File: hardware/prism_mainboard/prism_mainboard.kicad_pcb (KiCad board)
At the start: 6 copper layers, 100 x 100 mm, 76 parts, among them IC1 KTDM4G3C618BGIEAT, IC2 KTDM4G3C618BGIEAT, IC3 USB3320C-EZK, J1 503398-1892, U1 XC7Z015-2CLG485I, U2 LMS7002M, U3 PEC16-4220F-S0024, U4 AMS1117-1.8, U5 AMS1117-1.8, U6 AMS1117-1.8, U7 AMS1117-1.8

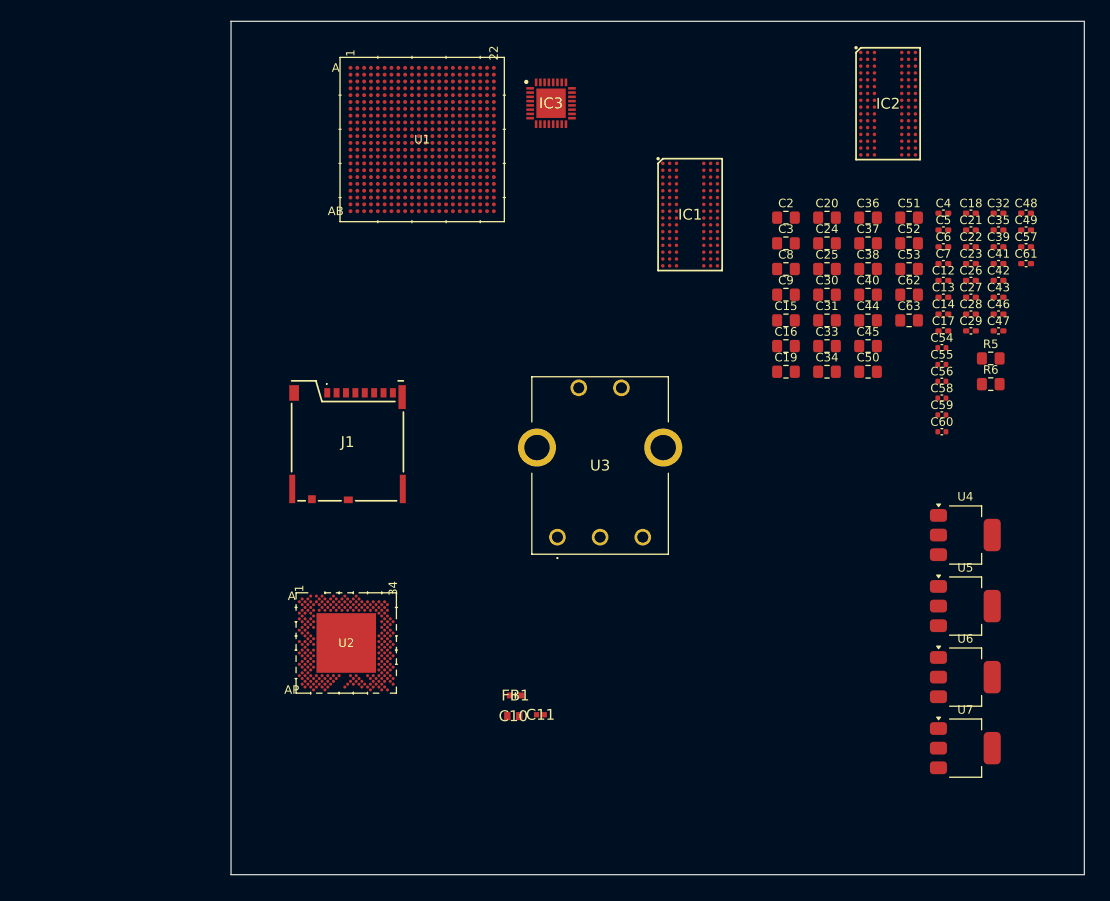
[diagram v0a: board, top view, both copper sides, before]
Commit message: Schematic and PCB Updates
Added Edge.cuts to max 100mm x 100mm size, just as a base, can shrink it if needed. Simple schematic labeling for memory and other necessary stuff.
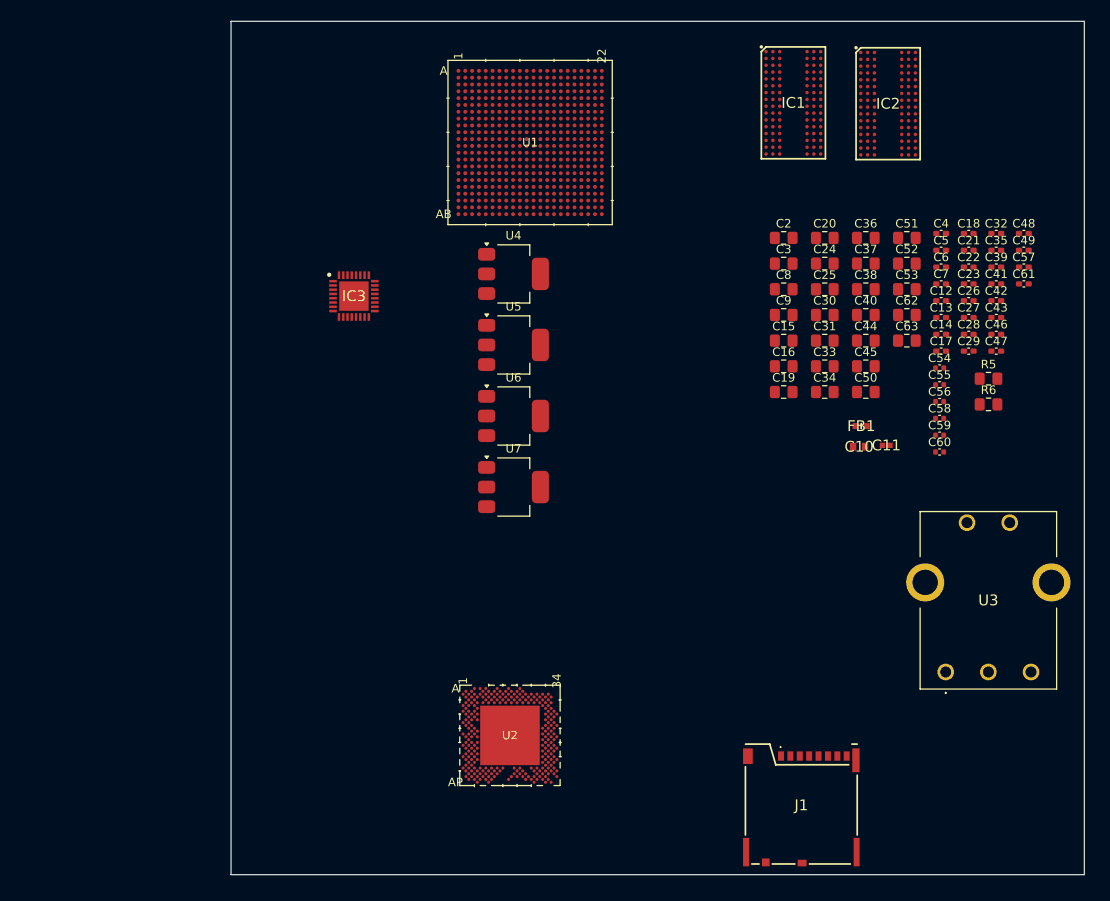
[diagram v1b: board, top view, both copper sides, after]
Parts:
- moved J1 68.1 mm to (137.9, 141.5)
- moved U5 61.2 mm to (110.8, 94.7)
- moved U6 61.2 mm to (110.8, 103.0)
- moved U4 61.2 mm to (110.8, 86.4)
- moved U7 61.2 mm to (110.8, 111.4)
- moved C11 51.4 mm to (154.4, 106.5)
- moved FB1 51.4 mm to (151.5, 104.2)
- moved C10 51.4 mm to (151.2, 106.7)
- moved U3 48.2 mm to (161.4, 133.1)
- moved IC3 32.3 mm to (92.0, 89.0)
- moved U2 22.0 mm to (110.3, 140.5)
- moved IC1 17.8 mm to (143.6, 66.3)
- moved U1 12.7 mm to (112.7, 71.0)
- moved C15 2.39 mm to (142.4, 94.2)
- moved C16 2.39 mm to (142.4, 97.2)
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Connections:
- IC1 pad A2: unconnected-(IC1-DQU5-PadA2) -> DQU5_0
- IC1 pad A3: unconnected-(IC1-DQU7-PadA3) -> DQU7_0
- IC1 pad A7: unconnected-(IC1-DQU4-PadA7) -> DQU4_0
- IC1 pad B7: unconnected-(IC1-~{DQSU}-PadB7) -> DQSUN_0
- IC1 pad B8: unconnected-(IC1-DQU6-PadB8) -> DQU6_0
- IC1 pad C2: unconnected-(IC1-DQU3-PadC2) -> DQU3_0
- IC1 pad C3: unconnected-(IC1-DQU1-PadC3) -> DQU1_0
- IC1 pad C7: unconnected-(IC1-DQSU-PadC7) -> DQSUP_0
- IC1 pad C8: unconnected-(IC1-DQU2-PadC8) -> DQU2_0
- IC1 pad D3: unconnected-(IC1-DMU-PadD3) -> DM1
- IC1 pad D7: unconnected-(IC1-DQU0-PadD7) -> DQU0_0
- IC1 pad E3: unconnected-(IC1-DQL0-PadE3) -> DQL0_0
- IC1 pad E7: unconnected-(IC1-DML-PadE7) -> DM0
- IC1 pad F2: unconnected-(IC1-DQL2-PadF2) -> DQL2_0
- IC1 pad F3: unconnected-(IC1-DQSL-PadF3) -> DQSLP_0
- IC1 pad F7: unconnected-(IC1-DQL1-PadF7) -> DQL1_0
- IC1 pad F8: unconnected-(IC1-DQL3-PadF8) -> DQL3_0
- IC1 pad G2: unconnected-(IC1-DQL6-PadG2) -> DQL6_0
- IC1 pad G3: unconnected-(IC1-~{DQSL}-PadG3) -> DQSLN_0
- IC1 pad H3: unconnected-(IC1-DQL4-PadH3) -> DQL4_0
- IC1 pad H7: unconnected-(IC1-DQL7-PadH7) -> DQL7_0
- IC1 pad H8: unconnected-(IC1-DQL5-PadH8) -> DQL5_0
- IC1 pad J3: unconnected-(IC1-~{RAS}-PadJ3) -> RAS
- IC1 pad J7: unconnected-(IC1-CK-PadJ7) -> CKP
- IC1 pad K1: unconnected-(IC1-ODT-PadK1) -> ODT
- IC1 pad K3: unconnected-(IC1-~{CAS}-PadK3) -> CAS
- IC1 pad K7: unconnected-(IC1-~{CK}-PadK7) -> CKN
- IC1 pad K9: unconnected-(IC1-CKE-PadK9) -> CKE
- IC1 pad L2: unconnected-(IC1-~{CS}-PadL2) -> CS
- IC1 pad L3: unconnected-(IC1-~{WE}-PadL3) -> WE
- IC1 pad L7: unconnected-(IC1-A10/AP-PadL7) -> A10
- IC1 pad M2: unconnected-(IC1-BA0-PadM2) -> BA0
- IC1 pad M3: unconnected-(IC1-BA2-PadM3) -> BA
- IC1 pad N2: unconnected-(IC1-A3-PadN2) -> A3
- IC1 pad N3: unconnected-(IC1-A0-PadN3) -> A0
- IC1 pad N7: unconnected-(IC1-A12/~{BC}-PadN7) -> A12
- IC1 pad N8: unconnected-(IC1-BA1-PadN8) -> BA1
- IC1 pad P2: unconnected-(IC1-A5-PadP2) -> A5
- IC1 pad P3: unconnected-(IC1-A2-PadP3) -> A2
- IC1 pad P7: unconnected-(IC1-A1-PadP7) -> A1
- IC1 pad P8: unconnected-(IC1-A4-PadP8) -> A4
- IC1 pad R2: unconnected-(IC1-A7-PadR2) -> A7
- IC1 pad R3: unconnected-(IC1-A9-PadR3) -> A9
- IC1 pad R7: unconnected-(IC1-A11-PadR7) -> A11
- IC1 pad R8: unconnected-(IC1-A6-PadR8) -> A6
- IC1 pad T3: unconnected-(IC1-A13-PadT3) -> A13
- IC1 pad T7: unconnected-(IC1-A14-PadT7) -> A14
- IC1 pad T8: unconnected-(IC1-A8-PadT8) -> A8
- IC2 pad A2: unconnected-(IC2-DQU5-PadA2) -> DQU5_1
- IC2 pad A3: unconnected-(IC2-DQU7-PadA3) -> DQU7_1
- IC2 pad A7: unconnected-(IC2-DQU4-PadA7) -> DQU4_1
- IC2 pad B7: unconnected-(IC2-~{DQSU}-PadB7) -> DQSUN_1
- IC2 pad B8: unconnected-(IC2-DQU6-PadB8) -> DQU6_1
- IC2 pad C2: unconnected-(IC2-DQU3-PadC2) -> DQU3_1
- IC2 pad C3: unconnected-(IC2-DQU1-PadC3) -> DQU1_1
- IC2 pad C7: unconnected-(IC2-DQSU-PadC7) -> DQSUP_1
- IC2 pad C8: unconnected-(IC2-DQU2-PadC8) -> DQU2_1
- IC2 pad D3: unconnected-(IC2-DMU-PadD3) -> DM3
- IC2 pad D7: unconnected-(IC2-DQU0-PadD7) -> DQU0_1
- IC2 pad E3: unconnected-(IC2-DQL0-PadE3) -> DQL0_1
- IC2 pad E7: unconnected-(IC2-DML-PadE7) -> DM2
- IC2 pad F2: unconnected-(IC2-DQL2-PadF2) -> DQL2_1
- IC2 pad F3: unconnected-(IC2-DQSL-PadF3) -> DQSLP_1
- IC2 pad F7: unconnected-(IC2-DQL1-PadF7) -> DQL1_1
- IC2 pad F8: unconnected-(IC2-DQL3-PadF8) -> DQL3_1
- IC2 pad G2: unconnected-(IC2-DQL6-PadG2) -> DQL6_1
- IC2 pad G3: unconnected-(IC2-~{DQSL}-PadG3) -> DQSLN_1
- IC2 pad H3: unconnected-(IC2-DQL4-PadH3) -> DQL4_1
- IC2 pad H7: unconnected-(IC2-DQL7-PadH7) -> DQL7_1
- IC2 pad H8: unconnected-(IC2-DQL5-PadH8) -> DQL5_1
- IC2 pad J3: unconnected-(IC2-~{RAS}-PadJ3) -> RAS
- IC2 pad J7: unconnected-(IC2-CK-PadJ7) -> CKP
- IC2 pad K1: unconnected-(IC2-ODT-PadK1) -> ODT
- IC2 pad K3: unconnected-(IC2-~{CAS}-PadK3) -> CAS
- IC2 pad K7: unconnected-(IC2-~{CK}-PadK7) -> CKN
- IC2 pad K9: unconnected-(IC2-CKE-PadK9) -> CKE
- IC2 pad L2: unconnected-(IC2-~{CS}-PadL2) -> CS
- IC2 pad L3: unconnected-(IC2-~{WE}-PadL3) -> WE
- IC2 pad L7: unconnected-(IC2-A10/AP-PadL7) -> A10
- IC2 pad M2: unconnected-(IC2-BA0-PadM2) -> BA0
- IC2 pad M3: unconnected-(IC2-BA2-PadM3) -> BA
- IC2 pad N2: unconnected-(IC2-A3-PadN2) -> A3
- IC2 pad N3: unconnected-(IC2-A0-PadN3) -> A0
- IC2 pad N7: unconnected-(IC2-A12/~{BC}-PadN7) -> A12
- IC2 pad N8: unconnected-(IC2-BA1-PadN8) -> BA1
- IC2 pad P2: unconnected-(IC2-A5-PadP2) -> A5
- IC2 pad P3: unconnected-(IC2-A2-PadP3) -> A2
- IC2 pad P7: unconnected-(IC2-A1-PadP7) -> A1
- IC2 pad P8: unconnected-(IC2-A4-PadP8) -> A4
- IC2 pad R2: unconnected-(IC2-A7-PadR2) -> A7
- IC2 pad R3: unconnected-(IC2-A9-PadR3) -> A9
- IC2 pad R7: unconnected-(IC2-A11-PadR7) -> A11
- IC2 pad R8: unconnected-(IC2-A6-PadR8) -> A6
- IC2 pad T3: unconnected-(IC2-A13-PadT3) -> A13
- IC2 pad T7: unconnected-(IC2-A14-PadT7) -> A14
- IC2 pad T8: unconnected-(IC2-A8-PadT8) -> A8
- U1 pad AA22: unconnected-(U1E-PS_DDR_DQ26_502-PadAA22) -> DQU2_1
- U1 pad B21: unconnected-(U1C-PS_DDR_DQ2_502-PadB21) -> DQL2_0
- U1 pad B22: unconnected-(U1C-PS_DDR_DM0_502-PadB22) -> DM0
- U1 pad C20: unconnected-(U1C-PS_DDR_DQ1_502-PadC20) -> DQL1_0
- U1 pad C21: unconnected-(U1C-PS_DDR_DQS_P0_502-PadC21) -> DQSLP_0
- U1 pad D20: unconnected-(U1C-PS_DDR_DQ3_502-PadD20) -> DQL3_0
- U1 pad D21: unconnected-(U1C-PS_DDR_DQS_N0_502-PadD21) -> DQSLN_0
- U1 pad D22: unconnected-(U1C-PS_DDR_DQ0_502-PadD22) -> DQL0_0
- U1 pad E20: unconnected-(U1C-PS_DDR_DQ4_502-PadE20) -> DQL4_0
- U1 pad E22: unconnected-(U1C-PS_DDR_DQ5_502-PadE22) -> DQL5_0
- U1 pad F16: unconnected-(U1C-PS_CLK_500-PadF16) -> CLK
- U1 pad F19: unconnected-(U1C-PS_DDR_A13_502-PadF19) -> A13
- U1 pad F21: unconnected-(U1C-PS_DDR_DQ6_502-PadF21) -> DQL6_0
- U1 pad F22: unconnected-(U1C-PS_DDR_DQ7_502-PadF22) -> DQL7_0
- U1 pad G18: unconnected-(U1C-PS_DDR_A11_502-PadG18) -> A11
- U1 pad G19: unconnected-(U1C-PS_DDR_A14_502-PadG19) -> A14
- U1 pad G21: unconnected-(U1C-PS_DDR_DQ8_502-PadG21) -> DQU0_0
- U1 pad G22: unconnected-(U1C-PS_DDR_DQ9_502-PadG22) -> DQU1_0
- U1 pad H18: unconnected-(U1D-PS_DDR_A9_502-PadH18) -> A9
- U1 pad H19: unconnected-(U1D-PS_DDR_A12_502-PadH19) -> A12
- U1 pad H21: unconnected-(U1D-PS_DDR_DQS_P1_502-PadH21) -> DQSUP_0
- U1 pad J16: unconnected-(U1D-PS_DDR_A6_502-PadJ16) -> A6
- U1 pad J17: unconnected-(U1D-PS_DDR_A7_502-PadJ17) -> A7
- U1 pad J18: unconnected-(U1D-PS_DDR_A8_502-PadJ18) -> A8
- U1 pad J20: unconnected-(U1D-PS_DDR_A10_502-PadJ20) -> A10
- U1 pad J21: unconnected-(U1D-PS_DDR_DQS_N1_502-PadJ21) -> DQSUN_0
- U1 pad J22: unconnected-(U1D-PS_DDR_DQ14_502-PadJ22) -> DQU6_0
- U1 pad K17: unconnected-(U1D-PS_DDR_A4_502-PadK17) -> A4
- U1 pad K18: unconnected-(U1D-PS_DDR_A5_502-PadK18) -> A5
- U1 pad K19: unconnected-(U1D-PS_DDR_A2_502-PadK19) -> A2
- U1 pad K20: unconnected-(U1D-PS_DDR_DQ15_502-PadK20) -> DQU7_0
- U1 pad K22: unconnected-(U1D-PS_DDR_DQ13_502-PadK22) -> DQU5_0
- U1 pad L16: unconnected-(U1D-PS_DDR_BA0_502-PadL16) -> BA0
- U1 pad L17: unconnected-(U1D-PS_DDR_BA1_502-PadL17) -> BA1
- U1 pad L19: unconnected-(U1D-PS_DDR_A3_502-PadL19) -> A3
- U1 pad L20: unconnected-(U1D-PS_DDR_DQ12_502-PadL20) -> DQU4_0
- U1 pad L21: unconnected-(U1D-PS_DDR_DQ11_502-PadL21) -> DQU3_0
- U1 pad L22: unconnected-(U1D-PS_DDR_DQ10_502-PadL22) -> DQU2_0
- U1 pad M17: unconnected-(U1D-PS_DDR_BA2_502-PadM17) -> BA2
- U1 pad M18: unconnected-(U1D-PS_DDR_A1_502-PadM18) -> A1
- U1 pad M19: unconnected-(U1D-PS_DDR_A0_502-PadM19) -> A0
- U1 pad M21: unconnected-(U1D-PS_DDR_DQ22_502-PadM21) -> DQL6_1
- U1 pad M22: unconnected-(U1D-PS_DDR_DQ16_502-PadM22) -> DQL0_1
- U1 pad N18: unconnected-(U1D-PS_DDR_CKN_502-PadN18) -> CKN
- U1 pad N19: unconnected-(U1D-PS_DDR_CKP_502-PadN19) -> CKP
- U1 pad N20: unconnected-(U1D-PS_DDR_DQ18_502-PadN20) -> DQL2_1
- U1 pad N21: unconnected-(U1D-PS_DDR_DQS_P2_502-PadN21) -> DQSLP_1
- U1 pad P17: unconnected-(U1D-PS_DDR_CS_B_502-PadP17) -> CS
- U1 pad P18: unconnected-(U1D-PS_DDR_ODT_502-PadP18) -> ODT
- U1 pad P20: unconnected-(U1D-PS_DDR_CAS_B_502-PadP20) -> CAS
- U1 pad P21: unconnected-(U1D-PS_DDR_DQS_N2_502-PadP21) -> DQSLN_1
- U1 pad P22: unconnected-(U1D-PS_DDR_DM2_502-PadP22) -> DM2
- U1 pad R18: unconnected-(U1E-PS_DDR_RAS_B_502-PadR18) -> RAS
- U1 pad R19: unconnected-(U1E-PS_DDR_WE_B_502-PadR19) -> WE
- U1 pad R20: unconnected-(U1E-PS_DDR_DQ20_502-PadR20) -> DQL4_1
- U1 pad R22: unconnected-(U1E-PS_DDR_DQ23_502-PadR22) -> DQL7_1
- U1 pad T19: unconnected-(U1E-PS_DDR_CKE_502-PadT19) -> CKE
- U1 pad T20: unconnected-(U1E-PS_DDR_DQ17_502-PadT20) -> DQL1_1
- U1 pad T21: unconnected-(U1E-PS_DDR_DQ21_502-PadT21) -> DQL5_1
- U1 pad T22: unconnected-(U1E-PS_DDR_DQ19_502-PadT22) -> DQL3_1
- U1 pad U21: unconnected-(U1E-PS_DDR_DQ27_502-PadU21) -> DQU3_1
- U1 pad U22: unconnected-(U1E-PS_DDR_DQ25_502-PadU22) -> DQU1_1
- U1 pad V20: unconnected-(U1E-PS_DDR_DQ30_502-PadV20) -> DQU6_1
- U1 pad V21: unconnected-(U1E-PS_DDR_DQS_P3_502-PadV21) -> DQSUP_1
- U1 pad W20: unconnected-(U1E-PS_DDR_DQ29_502-PadW20) -> DQU5_1
- U1 pad W21: unconnected-(U1E-PS_DDR_DQS_N3_502-PadW21) -> DQSUN_1
- U1 pad W22: unconnected-(U1E-PS_DDR_DQ28_502-PadW22) -> DQU4_1
- U1 pad Y20: unconnected-(U1E-PS_DDR_DQ24_502-PadY20) -> DQU0_1
- U1 pad Y22: unconnected-(U1E-PS_DDR_DQ31_502-PadY22) -> DQU7_1

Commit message: Schematic Updates
Added the LMS7002M to XC7Z015 connections, atleast the preliminary data connections.
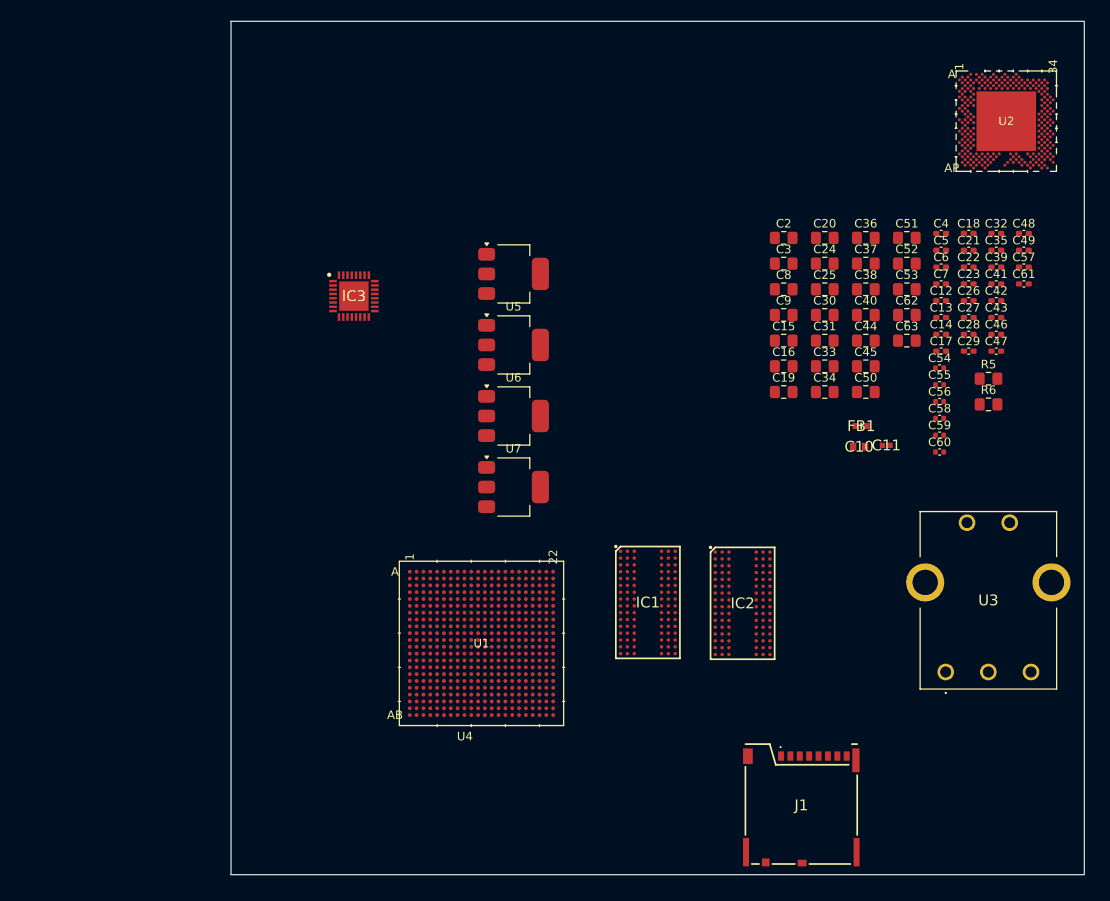
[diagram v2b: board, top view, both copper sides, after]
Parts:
- moved U2 92.5 mm to (168.5, 68.5)
- moved IC1 61.0 mm to (126.5, 124.9)
- moved IC2 61.0 mm to (137.6, 125.0)
- moved U1 59.0 mm to (107.0, 129.7)
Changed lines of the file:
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@@
 	(footprint "SamacSys_Parts:BGA96C80P9X16_750X1300X100"
 		(layer "F.Cu")
-		(at 154.65 66.45)
+		(at 137.6 125)
 		(descr "96 ball BGA-1")
 		(tags "Integrated Circuit")
@@
 		(tags "CMS SOT")
 		(property "Reference" "U4"
-			(at 0 -4.5 0)
+			(at -5.700001 54.200002 0)
 			(layer "F.SilkS")
 			(effects
@@
 	(footprint "LMS7002M:AQFN261_11P5X11P5_LIM"
 		(layer "F.Cu")
-		(at 110.336499 140.478501)
+		(at 168.5 68.5)
 		(tags "LMS7002M ")
 		(property "Reference" "U2"
@@
 	(footprint "SamacSys_Parts:BGA96C80P9X16_750X1300X100"
 		(layer "F.Cu")
-		(at 143.55 66.35)
+		(at 126.5 124.9)
 		(descr "96 ball BGA-1")
 		(tags "Integrated Circuit")
@@
 	(footprint "footprints:CLG485_XIL"
 		(layer "F.Cu")
-		(at 112.700001 70.999999)
+		(at 107 129.700001)
 		(tags "XC7Z015-2CLG485I ")
 		(property "Reference" "U1"

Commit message: Updates
Mostly Schematic updates, nothing too big. Added a few datasheets
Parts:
- added C1: T494D337K010AT, SamacSys_Parts:T494D, F.Cu at (149.8, 65.8)
- added J2: UJ32-21-C-H-G-HMT-LT-P24-TR, LIB_UJ32-21-C-H-G-HMT-LT-P24-TR:UJ3221CHGHMTLTP24TR, F.Cu at (87.2, 150.7)
- added R1: R, Resistor_SMD:R_0805_2012Metric_Pad1.20x1.40mm_HandSolder, F.Cu at (141.7, 63.6)
- added R2: R, Resistor_SMD:R_0805_2012Metric_Pad1.20x1.40mm_HandSolder, F.Cu at (141.7, 66.5)
- added R3: R, Resistor_SMD:R_0805_2012Metric_Pad1.20x1.40mm_HandSolder, F.Cu at (141.7, 69.5)
- added R4: R, Resistor_SMD:R_0805_2012Metric_Pad1.20x1.40mm_HandSolder, F.Cu at (151.4, 71.9)
- moved U7 44.4 mm to (121.5, 68.3), turned to 90 degrees
- moved IC1 39.2 mm to (133.2, 86.2)
- moved U6 34.8 mm to (113.1, 68.3), turned to 90 degrees
- moved U1 33.8 mm to (112.6, 96.4)
- moved U5 27.1 mm to (104.8, 68.3), turned to 90 degrees
- moved IC3 23.3 mm to (113.2, 79.3)
- moved U4 23.1 mm to (96.5, 68.3), turned to 90 degrees
- moved IC2 22.8 mm to (133.4, 102.5)
- moved C15 2.69 mm to (145.1, 94.2)
- moved C16 2.69 mm to (145.1, 97.2)
- moved C19 2.69 mm to (145.1, 100.2)
- moved C2 2.69 mm to (145.1, 82.2)
- moved C3 2.69 mm to (145.1, 85.2)
- moved C32 2.69 mm to (170.0, 81.7)
- moved C35 2.69 mm to (170.0, 83.6)
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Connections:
- IC3 pad 1: unconnected-(IC3-CLKOUT-Pad1) -> CLKOUT
- IC3 pad 10: unconnected-(IC3-DATA6-Pad10) -> USB_D6
- IC3 pad 13: unconnected-(IC3-DATA7-Pad13) -> USB_D7
- IC3 pad 18: unconnected-(IC3-DP-Pad18) -> Data+
- IC3 pad 19: unconnected-(IC3-DM-Pad19) -> Data-
- IC3 pad 2: unconnected-(IC3-NXT-Pad2) -> NXT
- IC3 pad 27: unconnected-(IC3-RESETB-Pad27) -> RST_B
- IC3 pad 29: unconnected-(IC3-STP-Pad29) -> STP
- IC3 pad 3: unconnected-(IC3-DATA0-Pad3) -> USB_D0
- IC3 pad 31: unconnected-(IC3-DIR-Pad31) -> DIR
- IC3 pad 4: unconnected-(IC3-DATA1-Pad4) -> USB_D1
- IC3 pad 5: unconnected-(IC3-DATA2-Pad5) -> USB_D2
- IC3 pad 6: unconnected-(IC3-DATA3-Pad6) -> USB_D3
- IC3 pad 7: unconnected-(IC3-DATA4-Pad7) -> USB_D4
- IC3 pad 9: unconnected-(IC3-DATA5-Pad9) -> USB_D5
- J1 pad 1: unconnected-(J1-DAT2-Pad1) -> SD_D2
- J1 pad 2: unconnected-(J1-CD/DAT3-Pad2) -> SD_D3
- J1 pad 3: unconnected-(J1-CMD-Pad3) -> SD_CMD
- J1 pad 5: unconnected-(J1-CLK-Pad5) -> SD_CLK
- J1 pad 6: unconnected-(J1-VSS-Pad6) -> GND
- J1 pad 7: unconnected-(J1-DAT0-Pad7) -> SD_D0
- J1 pad 8: unconnected-(J1-DAT1-Pad8) -> SD_D1
- U1 pad A11: unconnected-(U1B-PS_MIO28_501-PadA11) -> USB_D4
- U1 pad A12: unconnected-(U1B-PS_MIO30_501-PadA12) -> STP
- U1 pad A14: unconnected-(U1B-PS_MIO36_501-PadA14) -> CLKOUT
- U1 pad B11: unconnected-(U1C-PS_MIO34_501-PadB11) -> USB_D3
- U1 pad B12: unconnected-(U1C-PS_MIO43_501-PadB12) -> SD_D1
- U1 pad B14: unconnected-(U1C-PS_MIO45_501-PadB14) -> SD_D3
- U1 pad B9: unconnected-(U1A-PS_MIO37_501-PadB9) -> USB_D5
- U1 pad C10: unconnected-(U1C-PS_MIO39_501-PadC10) -> USB_D7
- U1 pad C15: unconnected-(U1C-PS_MIO41_501-PadC15) -> SD_CMD
- U1 pad C16: unconnected-(U1C-PS_MIO32_501-PadC16) -> USB_D0
- U1 pad C3: unconnected-(U1A-IO_L14N_T2_AD4N_SRCC_35-PadC3) -> FCLK1
- U1 pad D15: unconnected-(U1C-PS_MIO42_501-PadD15) -> SD_D0
- U1 pad D3: unconnected-(U1A-IO_L14P_T2_AD4P_SRCC_35-PadD3) -> MCLK1
- U1 pad D6: unconnected-(U1A-IO_L2N_T0_AD8N_35-PadD6) -> DIQ1_D4
- U1 pad D7: unconnected-(U1A-IO_L2P_T0_AD8P_35-PadD7) -> DIQ1_D5
- U1 pad D8: unconnected-(U1A-IO_L3N_T0_DQS_AD1N_35-PadD8) -> DIQ1_D6
- U1 pad E10: unconnected-(U1C-PS_MIO44_501-PadE10) -> SD_D2
- U1 pad E15: unconnected-(U1C-PS_MIO29_501-PadE15) -> DIR
- U1 pad E5: unconnected-(U1A-IO_L5N_T0_AD9N_35-PadE5) -> DIQ1_D10
- U1 pad E7: unconnected-(U1A-IO_L1N_T0_AD0N_35-PadE7) -> DIQ1_D2
- U1 pad E8: unconnected-(U1A-IO_L3P_T0_DQS_AD1P_35-PadE8) -> DIQ1_D7
- U1 pad E9: unconnected-(U1A-PS_MIO40_501-PadE9) -> SD_CLK
- U1 pad F10: unconnected-(U1C-PS_MIO38_501-PadF10) -> USB_D6
- U1 pad F14: unconnected-(U1C-PS_MIO31_501-PadF14) -> NXT
- U1 pad F5: unconnected-(U1A-IO_L5P_T0_AD9P_35-PadF5) -> DIQ1_D11
- U1 pad F6: unconnected-(U1A-IO_L6N_T0_VREF_35-PadF6) -> EN_IQSEL1
- U1 pad F7: unconnected-(U1A-IO_L1P_T0_AD0P_35-PadF7) -> DIQ1_D3
- U1 pad F9: unconnected-(U1A-PS_MIO35_501-PadF9) -> USB_D3
- U1 pad G11: unconnected-(U1C-PS_MIO33_501-PadG11) -> USB_D2
- U1 pad G6: unconnected-(U1A-IO_L6P_T0_35-PadG6) -> TXNRX1
- U1 pad G7: unconnected-(U1A-IO_L4N_T0_35-PadG7) -> DIQ1_D8
- U1 pad G8: unconnected-(U1A-IO_L4P_T0_35-PadG8) -> DIQ1_D9
- U1 pad H5: unconnected-(U1A-IO_25_35-PadH5) -> DIQ1_D1
- U1 pad H6: unconnected-(U1A-IO_0_35-PadH6) -> DIQ1_D0
- U1 pad H8: unconnected-(U1A-IO_0_34-PadH8) -> DIQ2_D0
- U1 pad J1: unconnected-(U1A-IO_L8N_T1_34-PadJ1) -> DIQ2_D10
- U1 pad J2: unconnected-(U1A-IO_L8P_T1_34-PadJ2) -> DIQ2_D11
- U1 pad J3: unconnected-(U1A-IO_L9P_T1_DQS_34-PadJ3) -> TXNRX2
- U1 pad J5: unconnected-(U1A-IO_L7P_T1_34-PadJ5) -> DIQ2_D9
- U1 pad J6: unconnected-(U1A-IO_L2N_T0_34-PadJ6) -> DIQ2_D3
- U1 pad J7: unconnected-(U1A-IO_L2P_T0_34-PadJ7) -> DIQ2_D4
- U1 pad J8: unconnected-(U1A-IO_L1P_T0_34-PadJ8) -> DIQ2_D2
- U1 pad K2: unconnected-(U1A-IO_L9N_T1_DQS_34-PadK2) -> EN_IQSEL2
- U1 pad K5: unconnected-(U1A-IO_L7N_T1_34-PadK5) -> DIQ2_D8
- U1 pad K7: unconnected-(U1A-IO_L3P_T0_DQS_PUDC_B_34-PadK7) -> DIQ2_D6
- U1 pad K8: unconnected-(U1A-IO_L1N_T0_34-PadK8) -> DIQ2_D1
- U1 pad L1: unconnected-(U1A-IO_L10N_T1_34-PadL1) -> SCLK
- U1 pad L2: unconnected-(U1A-IO_L10P_T1_34-PadL2) -> SEN
- U1 pad L4: unconnected-(U1A-IO_L12N_T1_MRCC_34-PadL4) -> FCLK2
- U1 pad L5: unconnected-(U1A-IO_L12P_T1_MRCC_34-PadL5) -> MCLK2
- U1 pad L6: unconnected-(U1A-IO_L4P_T0_34-PadL6) -> DIQ2_D7
- U1 pad L7: unconnected-(U1A-IO_L3N_T0_DQS_34-PadL7) -> DIQ2_D5
- U1 pad M1: unconnected-(U1B-IO_L15N_T2_DQS_34-PadM1) -> TXEN
- U1 pad M6: unconnected-(U1B-IO_L4N_T0_34-PadM6) -> SDO
- U1 pad M8: unconnected-(U1B-IO_L6P_T0_34-PadM8) -> RXEN
- U1 pad N8: unconnected-(U1B-IO_L5P_T0_34-PadN8) -> LM_RST
- U1 pad R8: unconnected-(U1B-IO_25_34-PadR8) -> SDIO
- U2 pad AA33: unconnected-(U2C-FCLK1-PadAA33) -> FCLK1
- U2 pad AB30: unconnected-(U2C-DIQ1_D10-PadAB30) -> DIQ1_D10
- U2 pad AB32: unconnected-(U2C-DIQ1_D11-PadAB32) -> DIQ1_D11
- U2 pad AB34: unconnected-(U2C-MCLK1-PadAB34) -> MCLK1
- U2 pad AC29: unconnected-(U2C-DIQ1_D5-PadAC29) -> DIQ1_D5
- U2 pad AC31: unconnected-(U2C-DIQ1_D8-PadAC31) -> DIQ1_D8
- U2 pad AC33: unconnected-(U2C-DIQ1_D9-PadAC33) -> DIQ1_D9
- U2 pad AD30: unconnected-(U2C-DIQ1_D4-PadAD30) -> DIQ1_D4
- U2 pad AD32: unconnected-(U2C-DIQ1_D7-PadAD32) -> DIQ1_D7
- U2 pad AE31: unconnected-(U2C-DIQ1_D3-PadAE31) -> DIQ1_D3
- U2 pad AE33: unconnected-(U2C-DIQ1_D6-PadAE33) -> DIQ1_D6
- U2 pad AF30: unconnected-(U2C-DIQ1_D1-PadAF30) -> DIQ1_D1
- U2 pad AF34: unconnected-(U2C-DIQ1_D2-PadAF34) -> DIQ1_D2
- U2 pad AG31: unconnected-(U2C-DIQ1_D0-PadAG31) -> DIQ1_D0
- U2 pad C27: unconnected-(U2B-SCL-PadC27) -> SCL
- U2 pad C29: unconnected-(U2B-SCLK-PadC29) -> SCLK
- U2 pad D26: unconnected-(U2B-SDA-PadD26) -> SDA
- U2 pad D28: unconnected-(U2B-SEN-PadD28) -> SEN
- U2 pad E27: unconnected-(U2B-RESET-PadE27) -> LM_RST
- U2 pad F28: unconnected-(U2B-SDO-PadF28) -> SDO
- U2 pad F30: unconnected-(U2B-SDIO-PadF30) -> SDIO
- U2 pad H30: unconnected-(U2B-DIQ2_D0-PadH30) -> DIQ2_D0
- U2 pad J31: unconnected-(U2B-DIQ2_D1-PadJ31) -> DIQ2_D1
- U2 pad K30: unconnected-(U2B-DIQ2_D2-PadK30) -> DIQ2_D2
- U2 pad K32: unconnected-(U2B-DIQ2_D3-PadK32) -> DIQ2_D3
- U2 pad K34: unconnected-(U2B-DIQ2_D5-PadK34) -> DIQ2_D5
- U2 pad L31: unconnected-(U2B-DIQ2_D4-PadL31) -> DIQ2_D4
- U2 pad M30: unconnected-(U2B-DIQ2_D6-PadM30) -> DIQ2_D6
- U2 pad M32: unconnected-(U2B-DIQ2_D7-PadM32) -> DIQ2_D7
- U2 pad N31: unconnected-(U2B-DIQ2_D8-PadN31) -> DIQ2_D8
- U2 pad N33: unconnected-(U2B-DIQ2_D9-PadN33) -> DIQ2_D9
- U2 pad P30: unconnected-(U2B-DIQ2_D10-PadP30) -> DIQ2_D10
- U2 pad P32: unconnected-(U2B-DIQ2_D11-PadP32) -> DIQ2_D11
- U2 pad P34: unconnected-(U2B-MCLK2-PadP34) -> MCLK2
- U2 pad R29: unconnected-(U2B-FCLK2-PadR29) -> FCLK2
- U2 pad R33: unconnected-(U2C-ENABLE__IQSEL2-PadR33) -> EN_IQSEL2
- U2 pad U29: unconnected-(U2C-TXEN-PadU29) -> TXEN
- U2 pad U31: unconnected-(U2C-TXNRX2-PadU31) -> TXNRX2
- U2 pad V32: unconnected-(U2C-TXNRX1-PadV32) -> TXNRX1
- U2 pad V34: unconnected-(U2C-RXEN-PadV34) -> RXEN
- U2 pad Y32: unconnected-(U2C-ENABLE_IQSEL1-PadY32) -> EN_IQSEL1
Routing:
- added copper zone on B.Cu, net GND
- added copper zone on In1.Cu, net GND
- added copper zone on In3.Cu, net GND
